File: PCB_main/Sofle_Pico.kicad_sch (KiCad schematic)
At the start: 68 parts, among them J1 Conn_02x08_Top_Bottom, J2 Conn_02x08_Top_Bottom, J3 Conn_01x06, SW1 SW_PUSH, SW10 SW_PUSH, SW11 SW_PUSH, SW12 SW_PUSH, SW13 SW_PUSH, SW14 SW_PUSH, SW15 SW_PUSH, SW16 SW_PUSH, SW17 SW_PUSH, SW18 SW_PUSH, SW2 SW_PUSH, SW20 SW_PUSH, SW21 SW_PUSH, SW22 SW_PUSH, SW23 SW_PUSH, SW24 SW_PUSH, SW27 SW_PUSH, SW28 SW_PUSH, SW29 SW_PUSH, SW3 SW_PUSH, SW30 SW_PUSH, SW37 SW_PUSH, SW38 SW_PUSH, SW39 SW_PUSH, SW4 SW_PUSH, SW40 SW_PUSH, SW41 SW_PUSH, SW5 SW_PUSH, SW6 SW_PUSH, SW7 SW_PUSH, SW8 SW_PUSH, SW9 SW_PUSH, U2 Pico

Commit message: improve positioning
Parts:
- J3: value Conn_01x06 -> Conn_02x03; footprint Connector_PinHeader_1.27mm:PinHeader_1x06_P1.27mm_Horizontal -> Connector_PinHeader_2.54mm:PinHeader_2x03_P2.54mm_Vertical; symbol Connector_Generic:Conn_01x06 -> Connector_Generic:Conn_02x03_Top_Bottom
- U2: footprint Module:RaspberryPi_Pico_SMD_HandSolder -> Module:RaspberryPi_Pico_SMD
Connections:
- net lcol0: now also J3.1 (Pin_1); no longer J3.2 (Pin_2)
- net lcol1: now also J3.2 (Pin_2); no longer J3.3 (Pin_3)
- net lcol2: now also J3.3 (Pin_3); no longer J3.4 (Pin_4)
- net lcol3: now also J3.4 (Pin_4); no longer J3.5 (Pin_5)
- net row5: now also J3.6 (Pin_6); no longer J3.1 (Pin_1)
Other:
- moved on the sheet: J3
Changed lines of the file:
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@@
 	(global_label "row5"
 		(shape input)
-		(at 31.75 31.75 180)
+		(at 44.45 39.37 0)
 		(effects
 			(font
 				(size 1.27 1.27)
 			)
-			(justify right)
+			(justify left)
 		)
 		(property "Intersheetrefs" "${INTERSHEET_REFS}"
-			(at 31.75 31.75 0)
+			(at 44.45 39.37 0)
 			(effects
 				(font
@@
 	(global_label "lcol3"
 		(shape input)
-		(at 31.75 41.91 180)
+		(at 44.45 34.29 0)
 		(effects
 			(font
 				(size 1.27 1.27)
 			)
-			(justify right)
+			(justify left)
 		)
 		(property "Intersheetrefs" "${INTERSHEET_REFS}"
-			(at 31.75 41.91 90)
+			(at 44.45 34.29 90)
 			(effects
 				(font
@@
 			)
 		)
-		(property "Footprint" "Module:RaspberryPi_Pico_SMD_HandSolder"
+		(property "Footprint" "Module:RaspberryPi_Pico_SMD"
 			(at 217.17 105.41 90)
 			(effects
@@
 	)
 	(symbol
-		(lib_id "Connector_Generic:Conn_01x06")
+		(lib_id "Connector_Generic:Conn_02x03_Top_Bottom")
 		(at 36.83 36.83 0)
 		(unit 1)
@@
 		(fields_autoplaced yes)
 		(property "Reference" "J3"
-			(at 39.37 36.8299 0)
+			(at 38.1 27.94 0)
 			(effects
 				(font
 					(size 1.27 1.27)
 				)
-				(justify left)
 			)
 		)
-		(property "Value" "Conn_01x06"
-			(at 39.37 39.3699 0)
+		(property "Value" "Conn_02x03"
+			(at 38.1 30.48 0)
 			(effects
 				(font
 					(size 1.27 1.27)
 				)
-				(justify left)
 			)
 		)
-		(property "Footprint" "Connector_PinHeader_1.27mm:PinHeader_1x06_P1.27mm_Horizontal"
+		(property "Footprint" "Connector_PinHeader_2.54mm:PinHeader_2x03_P2.54mm_Vertical"
 			(at 36.83 36.83 0)
 			(effects
@@
 			)
 		)
-		(property "Description" "Generic connector, single row, 01x06, script generated (kicad-library-utils/schlib/autogen/connector/)"
+		(property "Description" "Generic connector, double row, 02x03, top/bottom pin numbering scheme (row 1: 1...pins_per_row, row2: pins_per_row+1 ... num_pins), script generated (kicad-library-utils/schlib/autogen/connector/)"
 			(at 36.83 36.83 0)
 			(effects

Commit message: more pcb progress
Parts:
- J1, J2: footprint Connector_PinHeader_1.27mm:PinHeader_2x08_P1.27mm_Horizontal -> Connector_PinHeader_2.00mm:PinHeader_2x08_P2.00mm_Vertical; symbol Connector_Generic:Conn_02x08_Top_Bottom -> Connector_Generic:Conn_02x08_Odd_Even
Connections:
- net lcol0: now also J2.7 (Pin_7), U2.21 (GPIO16); no longer J2.1 (Pin_1), U2.1 (GPIO0)
- net lcol1: now also J2.6 (Pin_6), U2.22 (GPIO17); no longer J2.2 (Pin_2), U2.2 (GPIO1)
- net lcol2: now also J2.5 (Pin_5), U2.24 (GPIO18); no longer J2.3 (Pin_3), U2.4 (GPIO2)
- net lcol3: now also U2.25 (GPIO19); no longer U2.5 (GPIO3)
- net lcol4: now also J2.3 (Pin_3), U2.26 (GPIO20); no longer J2.5 (Pin_5), U2.6 (GPIO4)
- net lcol5: now also J2.2 (Pin_2), U2.27 (GPIO21); no longer J2.6 (Pin_6), U2.7 (GPIO5)
- net lcol6: now also J2.1 (Pin_1), U2.29 (GPIO22); no longer J2.7 (Pin_7), U2.9 (GPIO6)
- net rcol0: now also J1.7 (Pin_7), U2.20 (GPIO15); no longer J1.1 (Pin_1), U2.34 (GPIO28_ADC2)
- net rcol1: now also J1.6 (Pin_6), U2.19 (GPIO14); no longer J1.2 (Pin_2), U2.32 (GPIO27_ADC1)
- net rcol2: now also J1.5 (Pin_5), U2.17 (GPIO13); no longer J1.3 (Pin_3), U2.31 (GPIO26_ADC0)
- net rcol3: now also U2.16 (GPIO12); no longer U2.29 (GPIO22)
- net rcol4: now also J1.3 (Pin_3), U2.15 (GPIO11); no longer J1.5 (Pin_5), U2.27 (GPIO21)
- net rcol5: now also J1.2 (Pin_2), U2.14 (GPIO10); no longer J1.6 (Pin_6), U2.26 (GPIO20)
- net rcol6: now also J1.1 (Pin_1), U2.10 (GPIO7); no longer J1.7 (Pin_7), U2.25 (GPIO19)
- net row0: now also J1.16 (Pin_16), J2.16 (Pin_16), U2.1 (GPIO0); no longer J1.9 (Pin_9), J2.9 (Pin_9), U2.14 (GPIO10)
- net row1: now also J1.15 (Pin_15), J2.15 (Pin_15), U2.2 (GPIO1); no longer J1.10 (Pin_10), J2.10 (Pin_10), U2.15 (GPIO11)
- net row2: now also J1.14 (Pin_14), J2.14 (Pin_14), U2.4 (GPIO2); no longer U2.16 (GPIO12)
- net row3: now also J1.13 (Pin_13), J2.13 (Pin_13), U2.5 (GPIO3); no longer J1.11 (Pin_11), J1.12 (Pin_12), J2.11 (Pin_11), J2.12 (Pin_12), U2.17 (GPIO13)
- net row4: now also J1.12 (Pin_12), J2.12 (Pin_12), U2.6 (GPIO4); no longer J1.13 (Pin_13), J2.13 (Pin_13), U2.19 (GPIO14)
- net row5: now also J1.11 (Pin_11), J2.11 (Pin_11), U2.7 (GPIO5); no longer J1.14 (Pin_14), J2.14 (Pin_14), U2.20 (GPIO15)
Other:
- note removed: "TODO: make both halves part of the same matrix!!!"

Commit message: more
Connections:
- net lcol4: now also J3.5 (Pin_5)
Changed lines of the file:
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@@
+		)
+	)
+	(global_label "lcol4"
+		(shape input)
+		(at 44.45 36.83 0)
+		(effects
+			(font
+				(size 1.27 1.27)
+			)
+			(justify left)
+		)
+		(property "Intersheetrefs" "${INTERSHEET_REFS}"
+			(at 44.45 36.83 0)
+			(effects
+				(font
+					(size 1.27 1.27)
+				)
+				(hide yes)
+			)
 		)
 	)

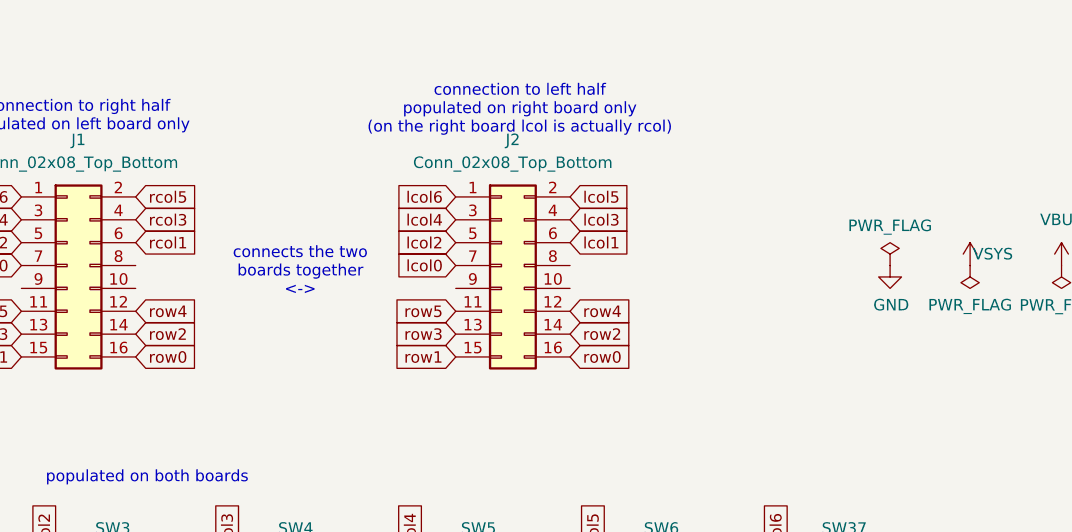
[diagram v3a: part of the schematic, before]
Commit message: rotate idc socket
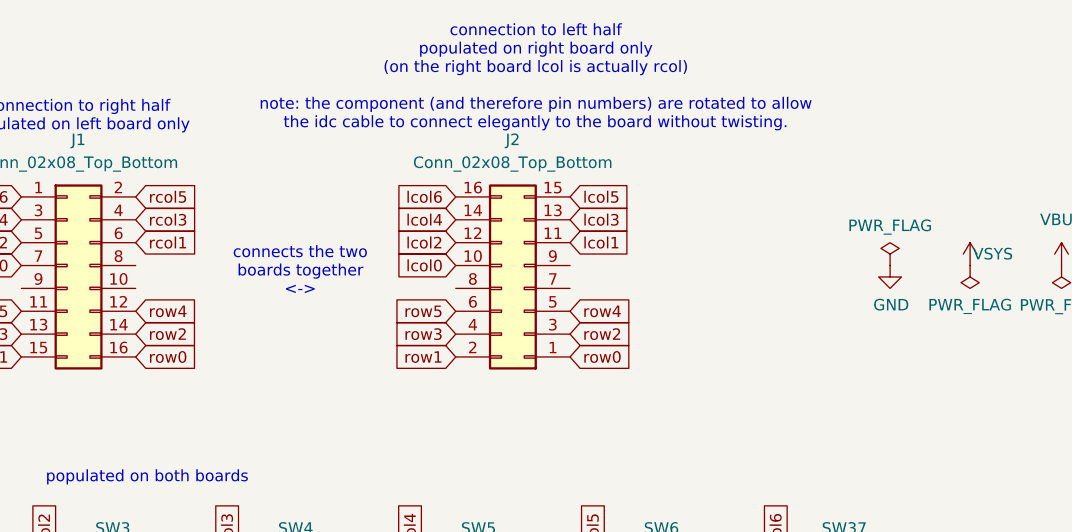
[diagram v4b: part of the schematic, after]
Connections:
- net lcol0: now also J2.10 (Pin_10); no longer J2.7 (Pin_7)
- net lcol1: now also J2.11 (Pin_11); no longer J2.6 (Pin_6)
- net lcol2: now also J2.12 (Pin_12); no longer J2.5 (Pin_5)
- net lcol3: now also J2.13 (Pin_13); no longer J2.4 (Pin_4)
- net lcol4: now also J2.14 (Pin_14); no longer J2.3 (Pin_3)
- net lcol5: now also J2.15 (Pin_15); no longer J2.2 (Pin_2)
- net lcol6: now also J2.16 (Pin_16); no longer J2.1 (Pin_1)
- net row0: now also J2.1 (Pin_1); no longer J2.16 (Pin_16)
- net row1: now also J2.2 (Pin_2); no longer J2.15 (Pin_15)
- net row2: now also J2.3 (Pin_3); no longer J2.14 (Pin_14)
- net row3: now also J2.4 (Pin_4); no longer J2.13 (Pin_13)
- net row4: now also J2.5 (Pin_5); no longer J2.12 (Pin_12)
- net row5: now also J2.6 (Pin_6); no longer J2.11 (Pin_11)
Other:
- note added: "connection to left half populated on right board only (on the right board lcol is actually rcol) note: the component (and therefore pin numbers) are rotated to allow the idc cable to connect elegantly to the board without twisting."
- note removed: "connection to left half populated on right board only (on the right board lcol is actually rcol)"
- moved on the sheet: J2
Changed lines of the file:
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@@
 		)
 	)
-	(text "connection to left half\npopulated on right board only\n(on the right board lcol is actually rcol)"
+	(text "connection to left half\npopulated on right board only\n(on the right board lcol is actually rcol)\n\nnote: the component (and therefore pin numbers) are rotated to allow\nthe idc cable to connect elegantly to the board without twisting."
 		(exclude_from_sim no)
-		(at 123.952 24.638 0)
+		(at 125.73 21.082 0)
 		(effects
 			(font
@@
 	(symbol
 		(lib_id "Connector_Generic:Conn_02x08_Odd_Even")
-		(at 121.92 41.91 0)
+		(at 124.46 44.45 180)
 		(unit 1)
 		(exclude_from_sim no)
@@
 		)
 		(property "Footprint" "Connector_PinHeader_2.00mm:PinHeader_2x08_P2.00mm_Vertical"
-			(at 121.92 41.91 0)
+			(at 124.46 44.45 0)
 			(effects
 				(font
@@
 		)
 		(property "Datasheet" "~"
-			(at 121.92 41.91 0)
+			(at 124.46 44.45 0)
 			(effects
 				(font
@@
 		)
 		(property "Description" "Generic connector, double row, 02x08, odd/even pin numbering scheme (row 1 odd numbers, row 2 even numbers), script generated (kicad-library-utils/schlib/autogen/connector/)"
-			(at 121.92 41.91 0)
+			(at 124.46 44.45 0)
 			(effects
 				(font

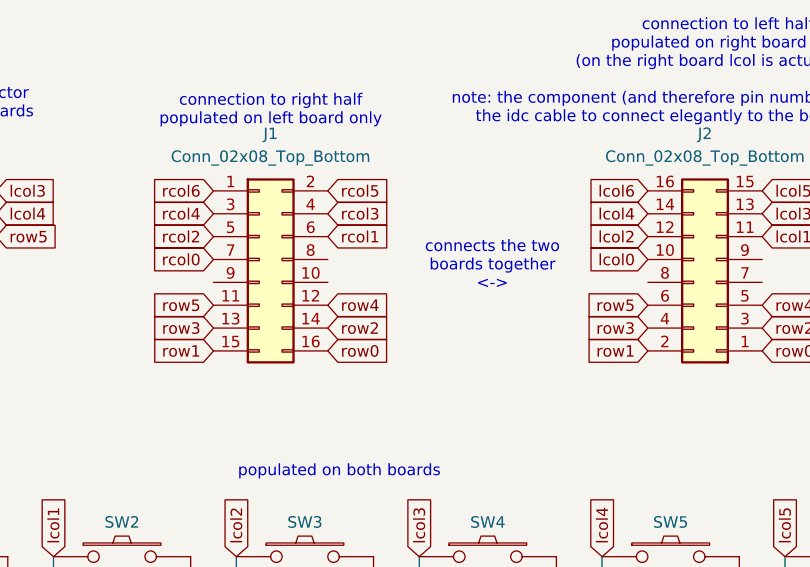
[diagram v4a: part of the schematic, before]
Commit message: adjust holes
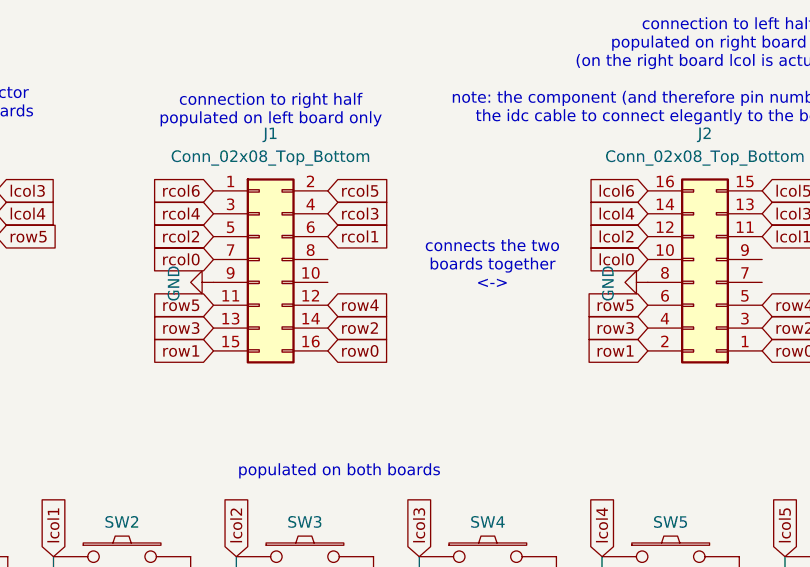
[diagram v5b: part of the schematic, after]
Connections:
- net GND: now also J1.9 (Pin_9), J2.8 (Pin_8)
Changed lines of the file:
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@@
+	)
+	(symbol
+		(lib_id "SofleKeyboard-rescue:GND-Lily58-cache-Lily58_Pro-rescue")
+		(at 116.84 44.45 270)
+		(unit 1)
+		(exclude_from_sim no)
+		(in_bom yes)
+		(on_board yes)
+		(dnp no)
+		(property "Reference" "#PWR02"
+			(at 110.49 44.45 0)
+			(effects
+				(font
+					(size 1.27 1.27)
+				)
+				(hide yes)
+			)
+		)
+		(property "Value" "GND"
+			(at 112.4458 44.577 0)
+			(effects
+				(font
+					(size 1.27 1.27)
+				)
+			)
+		)
+		(property "Footprint" ""
+			(at 116.84 44.45 0)
+			(effects
+				(font
+					(size 1.27 1.27)
+				)
+				(hide yes)
+			)
+		)
+		(property "Datasheet" ""
+			(at 116.84 44.45 0)
+			(effects
+				(font
+					(size 1.27 1.27)
+				)
+				(hide yes)
+			)
+		)
+		(property "Description" ""
+			(at 116.84 44.45 0)
+			(effects
+				(font
+					(size 1.27 1.27)
+				)
+				(hide yes)
+			)
+		)
+		(pin "1"
+		)
+		(instances
+			(project "Sofle_Pico"
+				(path "/06057b3a-55ab-4f4e-913e-2aeec5ff3587"
+					(reference "#PWR02")
+					(unit 1)
+				)
+			)
+		)
 	)
 	(symbol
@@
 					(unit 1)
 				)
+			)
+		)
+	)
+	(symbol
+		(lib_id "SofleKeyboard-rescue:GND-Lily58-cache-Lily58_Pro-rescue")
+		(at 68.58 44.45 270)
+		(unit 1)
+		(exclude_from_sim no)
+		(in_bom yes)
+		(on_board yes)
+		(dnp no)
+		(property "Reference" "#PWR03"
+			(at 62.23 44.45 0)
+			(effects
+				(font
+					(size 1.27 1.27)
+				)
+				(hide yes)
+			)
+		)
+		(property "Value" "GND"
+			(at 64.1858 44.577 0)
+			(effects
+				(font
+					(size 1.27 1.27)
+				)
+			)
+		)
+		(property "Footprint" ""
+			(at 68.58 44.45 0)
+			(effects
+				(font
+					(size 1.27 1.27)
+				)
+				(hide yes)
+			)
+		)
+		(property "Datasheet" ""
+			(at 68.58 44.45 0)
+			(effects
+				(font
+					(size 1.27 1.27)
+				)
+				(hide yes)
+			)
+		)
+		(property "Description" ""
+			(at 68.58 44.45 0)
+			(effects
+				(font
+					(size 1.27 1.27)
+				)
+				(hide yes)
+			)
+		)
+		(pin "1"
+		)
+		(instances
+			(project "Sofle_Pico"
+				(path "/06057b3a-55ab-4f4e-913e-2aeec5ff3587"
+					(reference "#PWR03")
+					(unit 1)
+				)

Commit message: thumb cluster connection uses idc
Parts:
- J3: footprint Connector_PinHeader_2.54mm:PinHeader_2x03_P2.54mm_Vertical -> Connector_PinHeader_2.00mm:PinHeader_2x03_P2.00mm_Vertical
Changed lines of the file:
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@@
 			)
 		)
-		(property "Footprint" "Connector_PinHeader_2.54mm:PinHeader_2x03_P2.54mm_Vertical"
+		(property "Footprint" "Connector_PinHeader_2.00mm:PinHeader_2x03_P2.00mm_Vertical"
 			(at 36.83 36.83 0)
 			(effects

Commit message: fix pcb
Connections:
- net GND: now also J2.9 (Pin_9); no longer J2.8 (Pin_8)
- net lcol0: now also J2.7 (Pin_7); no longer J2.10 (Pin_10)
- net lcol1: now also J2.6 (Pin_6); no longer J2.11 (Pin_11)
- net lcol2: now also J2.5 (Pin_5); no longer J2.12 (Pin_12)
- net lcol3: now also J2.4 (Pin_4); no longer J2.13 (Pin_13)
- net lcol4: now also J2.3 (Pin_3); no longer J2.14 (Pin_14)
- net lcol5: now also J2.2 (Pin_2); no longer J2.15 (Pin_15)
- net lcol6: now also J2.1 (Pin_1); no longer J2.16 (Pin_16)
- net row0: now also J2.16 (Pin_16), U2.9 (GPIO6); no longer J2.1 (Pin_1), U2.1 (GPIO0)
- net row1: now also J2.15 (Pin_15), U2.7 (GPIO5); no longer J2.2 (Pin_2), U2.2 (GPIO1)
- net row2: now also J2.14 (Pin_14), U2.6 (GPIO4); no longer J2.3 (Pin_3), U2.4 (GPIO2)
- net row3: now also J2.13 (Pin_13); no longer J2.4 (Pin_4)
- net row4: now also J2.12 (Pin_12), U2.4 (GPIO2); no longer J2.5 (Pin_5), U2.6 (GPIO4)
- net row5: now also J2.11 (Pin_11), U2.2 (GPIO1); no longer J2.6 (Pin_6), U2.7 (GPIO5)
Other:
- note added: "connection to left half populated on right board only (on the right board lcol is actually rcol)"
- note removed: "connection to left half populated on right board only (on the right board lcol is actually rcol) note: the component (and therefore pin numbers) are rotated to allow the idc cable to connect elegantly to the board without twisting."
- moved on the sheet: J2
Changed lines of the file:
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@@
 		)
 	)
-	(text "connection to left half\npopulated on right board only\n(on the right board lcol is actually rcol)\n\nnote: the component (and therefore pin numbers) are rotated to allow\nthe idc cable to connect elegantly to the board without twisting."
+	(text "connection to left half\npopulated on right board only\n(on the right board lcol is actually rcol)"
 		(exclude_from_sim no)
-		(at 125.73 21.082 0)
+		(at 123.698 23.114 0)
 		(effects
 			(font
@@
 		)
 	)
-	(global_label "lcol5"
+	(global_label "row2"
 		(shape input)
-		(at 129.54 34.29 0)
+		(at 199.39 93.98 180)
+		(fields_autoplaced yes)
 		(effects
 			(font
 				(size 1.27 1.27)
 			)
-			(justify left)
+			(justify right)
 		)
 		(property "Intersheetrefs" "${INTERSHEET_REFS}"
-			(at 129.54 34.29 0)
+			(at 192.5838 93.98 0)
 			(effects
 				(font
 					(size 1.27 1.27)
 				)
-				(justify left)
+				(justify right)
 				(hide yes)
 			)
 		)
 	)
-	(global_label "row4"
+	(global_label "lcol5"
 		(shape input)
-		(at 199.39 93.98 180)
-		(fields_autoplaced yes)
+		(at 129.54 34.29 0)
 		(effects
 			(font
 				(size 1.27 1.27)
 			)
-			(justify right)
+			(justify left)
 		)
 		(property "Intersheetrefs" "${INTERSHEET_REFS}"
-			(at 192.5838 93.98 0)
+			(at 129.54 34.29 0)
 			(effects
 				(font
 					(size 1.27 1.27)
 				)
-				(justify right)
+				(justify left)
 				(hide yes)
 			)
@@
 		)
 	)
+	(global_label "row5"
+		(shape input)
+		(at 199.39 83.82 180)
+		(fields_autoplaced yes)
+		(effects
+			(font
+				(size 1.27 1.27)
+			)
+			(justify right)
+		)
+		(property "Intersheetrefs" "${INTERSHEET_REFS}"
+			(at 192.5838 83.82 0)
+			(effects
+				(font
+					(size 1.27 1.27)
+				)
+				(justify right)
+				(hide yes)
+			)
+		)
+	)
 	(global_label "row3"
 		(shape input)
@@
 		)
 	)
+	(global_label "row0"
+		(shape input)
+		(at 199.39 101.6 180)
+		(fields_autoplaced yes)
+		(effects
+			(font
+				(size 1.27 1.27)
+			)
+			(justify right)
+		)
+		(property "Intersheetrefs" "${INTERSHEET_REFS}"
+			(at 192.5838 101.6 0)
+			(effects
+				(font
+					(size 1.27 1.27)
+				)
+				(justify right)
+				(hide yes)
+			)
+		)
+	)
 	(global_label "row5"
 		(shape input)
@@
 		)
 	)
-	(global_label "row0"
-		(shape input)
-		(at 199.39 81.28 180)
-		(fields_autoplaced yes)
-		(effects
-			(font
-				(size 1.27 1.27)
-			)
-			(justify right)
-		)
-		(property "Intersheetrefs" "${INTERSHEET_REFS}"
-			(at 192.5838 81.28 0)
-			(effects
-				(font
-					(size 1.27 1.27)
-				)
-				(justify right)
-				(hide yes)
-			)
-		)
-	)
 	(global_label "lcol0"
 		(shape input)
@@
 		)
 	)
-	(global_label "row5"
+	(global_label "rcol5"
 		(shape input)
-		(at 199.39 96.52 180)
+		(at 199.39 114.3 180)
 		(fields_autoplaced yes)
 		(effects
@@
 		)
 		(property "Intersheetrefs" "${INTERSHEET_REFS}"
-			(at 192.5838 96.52 0)
+			(at 192.1605 114.3 0)
 			(effects
 				(font
@@
 		)
 	)
-	(global_label "rcol5"
+	(global_label "row1"
 		(shape input)
-		(at 199.39 114.3 180)
+		(at 199.39 96.52 180)
 		(fields_autoplaced yes)
 		(effects
@@
 		)
 		(property "Intersheetrefs" "${INTERSHEET_REFS}"
-			(at 192.1605 114.3 0)
+			(at 192.5838 96.52 0)
 			(effects
 				(font
@@
 	(global_label "row4"
 		(shape input)
-		(at 81.28 46.99 0)
+		(at 199.39 88.9 180)
 		(fields_autoplaced yes)
 		(effects
@@
 				(size 1.27 1.27)
 			)
-			(justify left)
-		)
-		(property "Intersheetrefs" "${INTERSHEET_REFS}"
-			(at 88.0862 46.99 0)
-			(effects
-				(font
-					(size 1.27 1.27)
-				)
-				(justify left)
-				(hide yes)
-			)
-		)
-	)
-	(global_label "row1"
-		(shape input)
-		(at 27.94 99.06 180)
-		(effects
-			(font
-				(size 1.27 1.27)
-			)
 			(justify right)
 		)
 		(property "Intersheetrefs" "${INTERSHEET_REFS}"
-			(at 27.94 99.06 0)
+			(at 192.5838 88.9 0)
 			(effects
 				(font
 					(size 1.27 1.27)
 				)
+				(justify right)
 				(hide yes)
 			)
 		)
 	)
-	(global_label "rcol1"
+	(global_label "row4"
 		(shape input)
-		(at 199.39 127 180)
+		(at 81.28 46.99 0)
 		(fields_autoplaced yes)
 		(effects
@@
 				(size 1.27 1.27)
 			)
-			(justify right)
+			(justify left)
 		)
 		(property "Intersheetrefs" "${INTERSHEET_REFS}"
-			(at 192.1605 127 0)
+			(at 88.0862 46.99 0)
 			(effects
 				(font
 					(size 1.27 1.27)
 				)
-				(justify right)
+				(justify left)
 				(hide yes)
 			)
 		)
 	)
-	(global_label "rcol4"
+	(global_label "row1"
 		(shape input)
-		(at 199.39 116.84 180)
-		(fields_autoplaced yes)
+		(at 27.94 99.06 180)
 		(effects
 			(font
@@
 		)
 		(property "Intersheetrefs" "${INTERSHEET_REFS}"
-			(at 192.1605 116.84 0)
+			(at 27.94 99.06 0)
 			(effects
 				(font
 					(size 1.27 1.27)
 				)
-				(justify right)
 				(hide yes)
 			)
 		)
 	)
-	(global_label "row1"
+	(global_label "rcol1"
 		(shape input)
-		(at 199.39 83.82 180)
+		(at 199.39 127 180)
 		(fields_autoplaced yes)
 		(effects
@@
 		)
 		(property "Intersheetrefs" "${INTERSHEET_REFS}"
-			(at 192.5838 83.82 0)
+			(at 192.1605 127 0)
 			(effects
 				(font
@@
 		)
 	)
-	(global_label "row2"
+	(global_label "rcol4"
 		(shape input)
-		(at 199.39 88.9 180)
+		(at 199.39 116.84 180)
 		(fields_autoplaced yes)
 		(effects
@@
 		)
 		(property "Intersheetrefs" "${INTERSHEET_REFS}"
-			(at 192.5838 88.9 0)
+			(at 192.1605 116.84 0)
 			(effects
 				(font
@@
 	(symbol
 		(lib_id "Connector_Generic:Conn_02x08_Odd_Even")
-		(at 124.46 44.45 180)
+		(at 121.92 41.91 0)
 		(unit 1)
 		(exclude_from_sim no)
@@
 		)
 		(property "Footprint" "Connector_PinHeader_2.00mm:PinHeader_2x08_P2.00mm_Vertical"
-			(at 124.46 44.45 0)
+			(at 121.92 41.91 0)
 			(effects
 				(font
@@
 		)
 		(property "Datasheet" "~"
-			(at 124.46 44.45 0)
+			(at 121.92 41.91 0)
 			(effects
 				(font
@@
 		)
 		(property "Description" "Generic connector, double row, 02x08, odd/even pin numbering scheme (row 1 odd numbers, row 2 even numbers), script generated (kicad-library-utils/schlib/autogen/connector/)"
-			(at 124.46 44.45 0)
+			(at 121.92 41.91 0)
 			(effects
 				(font
